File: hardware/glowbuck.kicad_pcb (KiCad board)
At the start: 4 copper layers, 80 x 50 mm, 126 parts, among them J1 Conn_01x04_Socket, J105 Conn_01x01_Pin, J106 Conn_01x01_Pin, J107 Conn_01x01_Pin, J201 USB_C_Receptacle_USB2.0_16P, J202 USB_C_Receptacle_USB2.0_16P, J3 Conn_02x08_Counter_Clockwise, Q401 2N7002NXAKR, SW101 SW_Push, SW102 SW_Push, U101 ESP32-S3-WROOM-1, U102 SN74LVC1T45DBV, U103 INA181A3, U201 TPS25730D, U202 TPD2E2U06DCK, U301 AP63203WU, U401 SIC437A

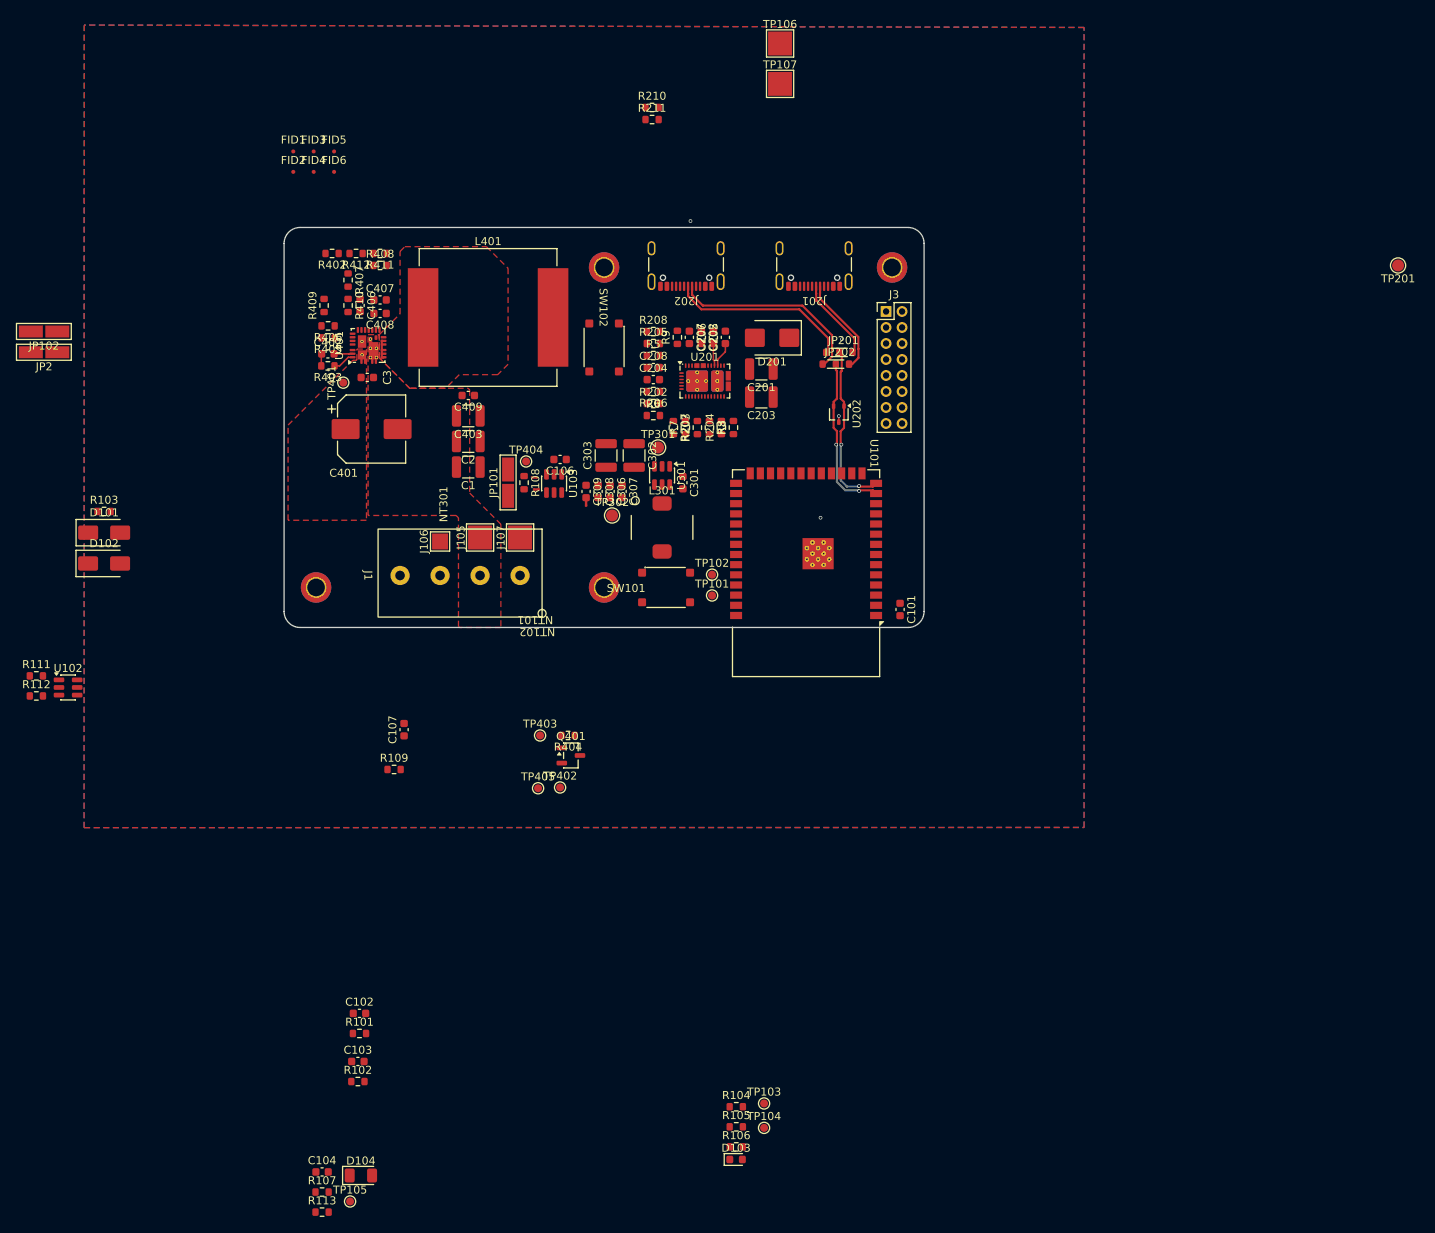
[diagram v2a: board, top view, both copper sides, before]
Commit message: Layout in progress. I2C done
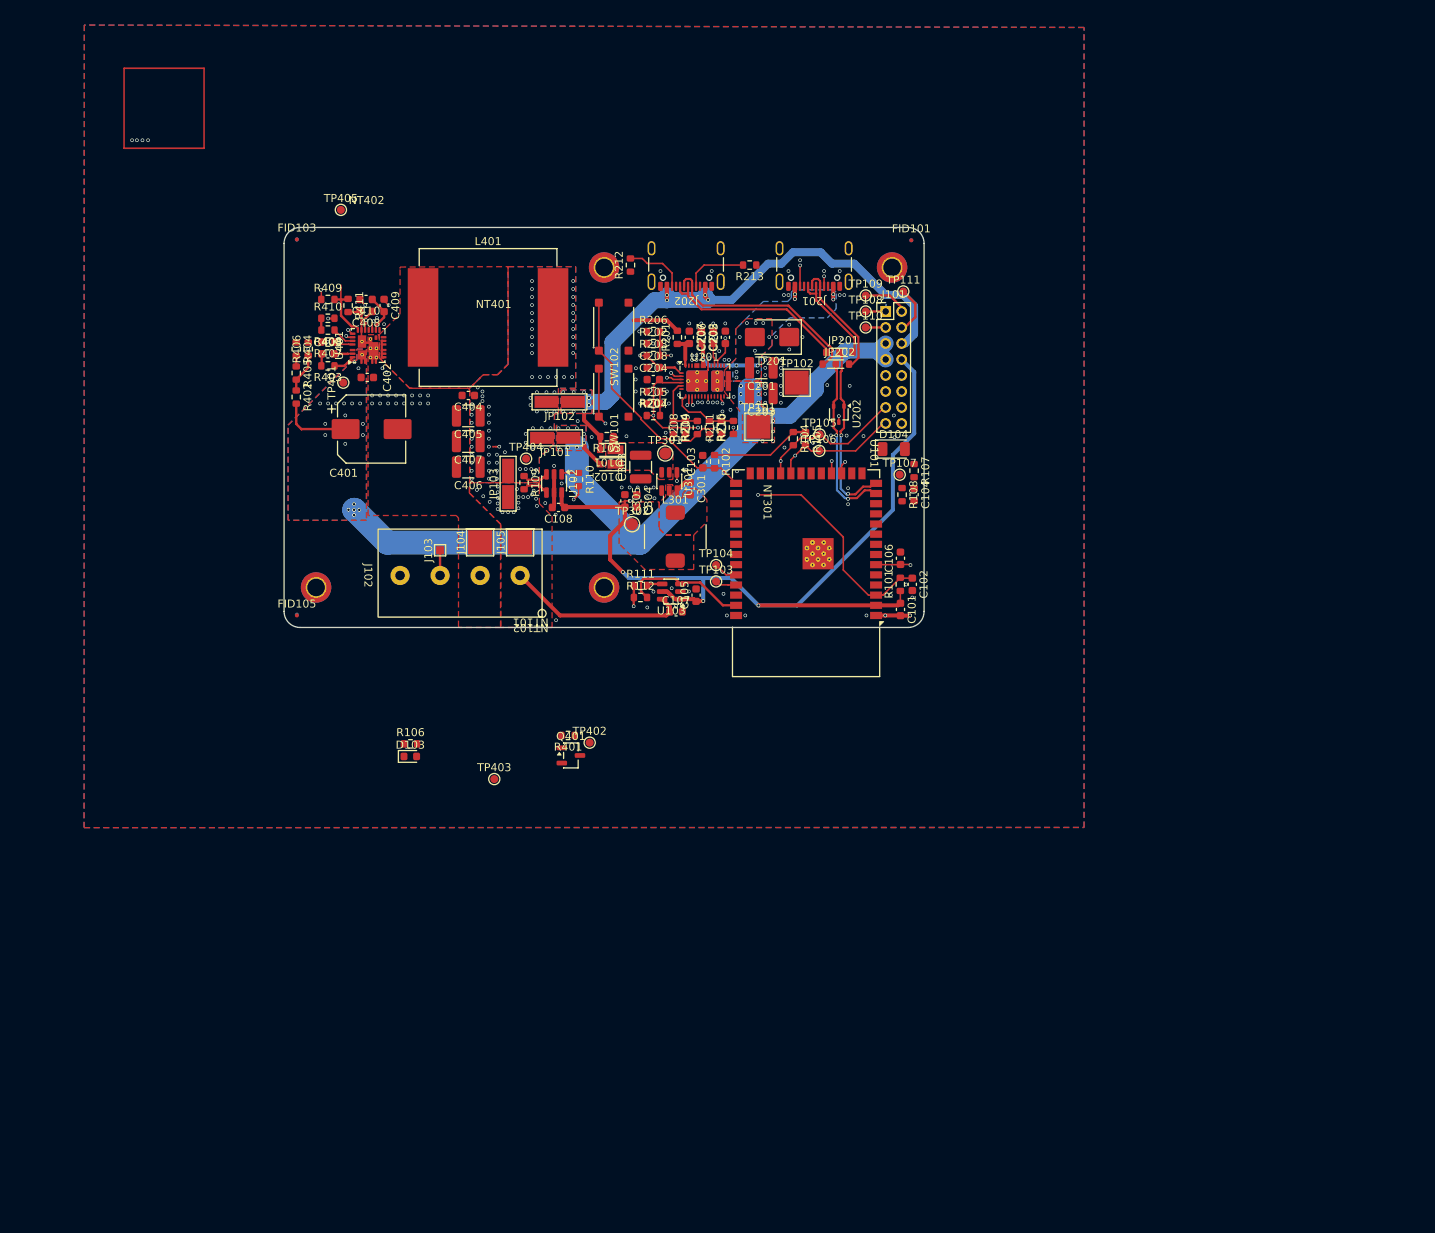
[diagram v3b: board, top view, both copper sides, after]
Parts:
- removed C302: 10u, Capacitor_SMD:C_1210_3225Metric
- removed C308, C309: 10u, Capacitor_SMD:C_0603_1608Metric
- removed J3: Conn_02x08_Counter_Clockwise, Connector_PinHeader_2.00mm:PinHeader_2x08_P2.00mm_Vertical
- removed TP201: TestPoint, TestPoint:TestPoint_Pad_D1.5mm
- added C105: 100n, Capacitor_SMD:C_0603_1608Metric, F.Cu at (105.5, 96.0)
- added C107: 100n, Capacitor_SMD:C_0603_1608Metric, F.Cu at (103.0, 98.0)
- added J101: Conn_02x08_Odd_Even, Connector_PinHeader_2.00mm:PinHeader_2x08_P2.00mm_Vertical, F.Cu at (129.2, 60.5)
- added NT401: NetTie_2, glowbuck:NETTIE_0.2mm, F.Cu at (80.3, 77.4)
- added NT402: NetTie_2, glowbuck:NETTIE_0.3mm, F.Cu at (64.4, 64.4)
- added TP108: TestPoint, TestPoint:TestPoint_Pad_D1.0mm, F.Cu at (126.7, 60.5)
- added TP109: TestPoint, TestPoint:TestPoint_Pad_D1.0mm, F.Cu at (126.7, 58.5)
- added TP110: TestPoint, TestPoint:TestPoint_Pad_D1.0mm, F.Cu at (126.7, 62.5)
- added TP111: TestPoint, TestPoint:TestPoint_Pad_D1.0mm, F.Cu at (131.4, 58.0)
- D101, D102: value SS34 -> MSS1P4-M3/89A; footprint Diode_SMD:D_SMA -> Diode_SMD:D_MicroSMP_AK
- FID102: renamed from FID4; moved to B.Cu
- FID104: renamed from FID5; moved to B.Cu
- FID106: renamed from FID6; moved to B.Cu
- J103: renamed from J106; footprint TestPoint:TestPoint_Pad_2.0x2.0mm -> TestPoint:TestPoint_Pad_1.0x1.0mm
- moved R107 118.6 mm to (132.8, 80.4), turned to -90 degrees
- moved TP107 113.9 mm to (130.9, 80.9)
- moved R108 113.4 mm to (131.2, 83.4), turned to -90 degrees
- moved D104 112.6 mm to (130.2, 77.7)
- moved C104 112.4 mm to (132.8, 83.4), turned to -90 degrees
- moved R102 89.4 mm to (107.8, 79.3), turned to -90 degrees
- moved R101 87.9 mm to (131.0, 94.6), turned to 90 degrees
- moved C102 87.5 mm to (132.5, 94.6), turned to -90 degrees
- moved C103 86.5 mm to (106.3, 79.3), turned to 90 degrees
- moved R105 86.5 mm to (119.2, 76.4), turned to -90 degrees
- moved TP106 84.9 mm to (120.9, 77.9)
- moved TP105 83.9 mm to (121.0, 75.9)
- moved R104 83.8 mm to (117.7, 76.4), turned to -90 degrees
- moved FID101 78.0 mm to (132.4, 51.6)
- moved R112 76.5 mm to (98.5, 96.2)
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- renumbered C107 to C106, C106 to C108, C307 to C304, C306 to C305, C3 to C402, C402 to C403, C409 to C404, C403 to C405, C1 to C406, C2 to C407, C406 to C408, C407 to C409, C408 to C410, FID1 to FID101, FID2 to FID103, FID3 to FID105, H1 to H101, H2 to H102, H3 to H103, H4 to H104, J1 to J102, J105 to J104, J107 to J105, JP2 to JP101, JP101 to JP103, R113 to R107, R107 to R108, R108 to R109, R109 to R110, R9 to R201, R205 to R202, R5 to R203, R6 to R204, R202 to R205, R208 to R206, R206 to R207, R7 to R208, R203 to R209, R8 to R210, R204 to R211, R210 to R212, R211 to R213, R207 to R214, R3 to R215, R404 to R401, R411 to R404, R412 to R405, R408 to R406, R405 to R407, R406 to R408, R407 to R409, R409 to R410, R410 to R411, TP106 to TP101, TP107 to TP102, TP101 to TP103, TP102 to TP104, TP103 to TP105, TP104 to TP106, TP105 to TP107, U103 to U102, U102 to U103
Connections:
- R409 pad 1: VOUT -> Net-(U401-V_{OUT})
- U101 pad 17: unconnected-(U101-IO9-Pad17) -> GPIO9
- U101 pad 18: unconnected-(U101-IO10-Pad18) -> GPIO10
- U101 pad 19: unconnected-(U101-IO11-Pad19) -> LIGHT_SENSE
- U101 pad 22: unconnected-(U101-IO14-Pad22) -> SCK
- U101 pad 23: unconnected-(U101-IO21-Pad23) -> SDA
- U101 pad 34: SDA -> unconnected-(U101-IO41-Pad34)
- U101 pad 35: SCK -> unconnected-(U101-IO42-Pad35)
- U101 pad 38: LIGHT_SENSE -> unconnected-(U101-IO2-Pad38)
- U101 pad 4: GPIO4 -> unconnected-(U101-IO4-Pad4)
- U101 pad 5: GPIO5 -> unconnected-(U101-IO5-Pad5)
- U103 pad 6: VOUT -> /LED_POW
- U401 pad 18: VOUT -> Net-(U401-V_{OUT})
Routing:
- net +3V3: track 0.00 -> 126.6 mm, vias 0 -> 3
- net VBUS: track 0.00 -> 112.9 mm, vias 0 -> 40
- net Net-(U401-V_{OUT}): track 0.00 -> 75.6 mm, vias 0 -> 3
- net +5V: track 0.00 -> 71.2 mm, vias 0 -> 12
- net /MC_EN: track 0.00 -> 59.3 mm, vias 0 -> 2
- net CURSENSE_V: track 0.00 -> 53.1 mm, vias 0 -> 2
- net SDA: track 0.00 -> 37.9 mm, vias 0 -> 2
- net SCK: track 0.00 -> 35.8 mm, vias 0 -> 2
- net /LED_D0: track 0.00 -> 32.1 mm, vias 0 -> 1
- net /MC_BOOT0: track 0.00 -> 32.0 mm
- net /USB-C and PD/PD_LDO1V5: track 0.00 -> 31.4 mm, vias 0 -> 4
- net /USB-C and PD/PD_LDO_3V3: track 0.00 -> 31.2 mm, vias 0 -> 6
- net /LED_POW: track 0.00 -> 23.0 mm, vias 0 -> 21
- net /USB-C and PD/USB_CC2: track 2.82 -> 21.4 mm, vias 0 -> 2
- net /USB-C and PD/USB_CC1: track 3.16 -> 20.9 mm, vias 0 -> 2
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- added copper zone on F.Cu, net +3V3
- added copper zone on B.Cu, net +5V
- added copper zone on F.Cu, net +5V
- added copper zone on F.Cu, net /Buck 3V3/SW
- added copper zone on F.Cu, net /Buck 3V3/VIN
- added copper zone on F.Cu, net /LED_POW
- added copper zone on B.Cu, net /USB-C and PD/VBUS_IN
- added copper zone on F.Cu, net /USB-C and PD/VBUS_IN
- added copper zone on B.Cu, net VBUS
- added copper zone on In2.Cu, net VBUS
- added copper zone on B.Cu, net VOUT
- added copper zone on F.Cu, net VOUT
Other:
- board text added: "glowbuck"
- board text added: "v1|Designed by Diamantenmine Manual & project files: github.com/Diamantenmine/glowbuck"

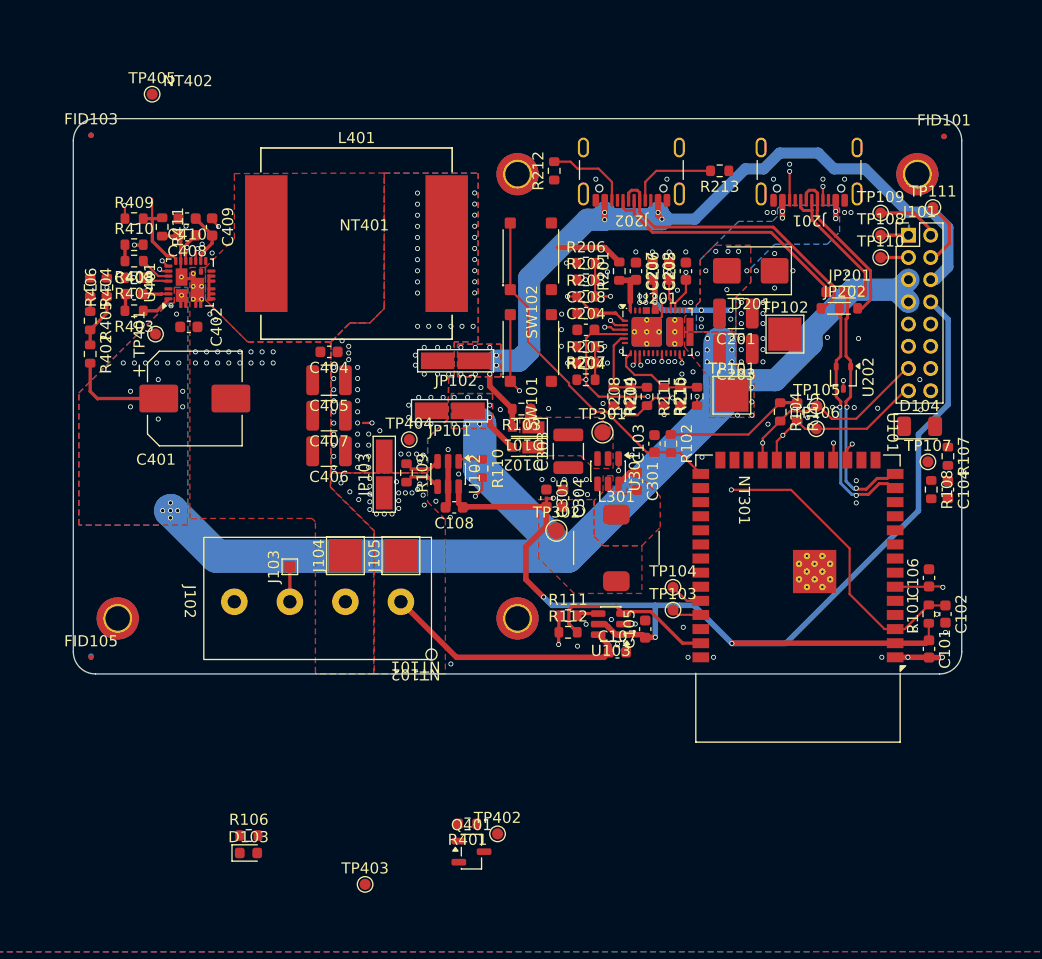
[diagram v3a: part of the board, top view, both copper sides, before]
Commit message: Fixed drc errors
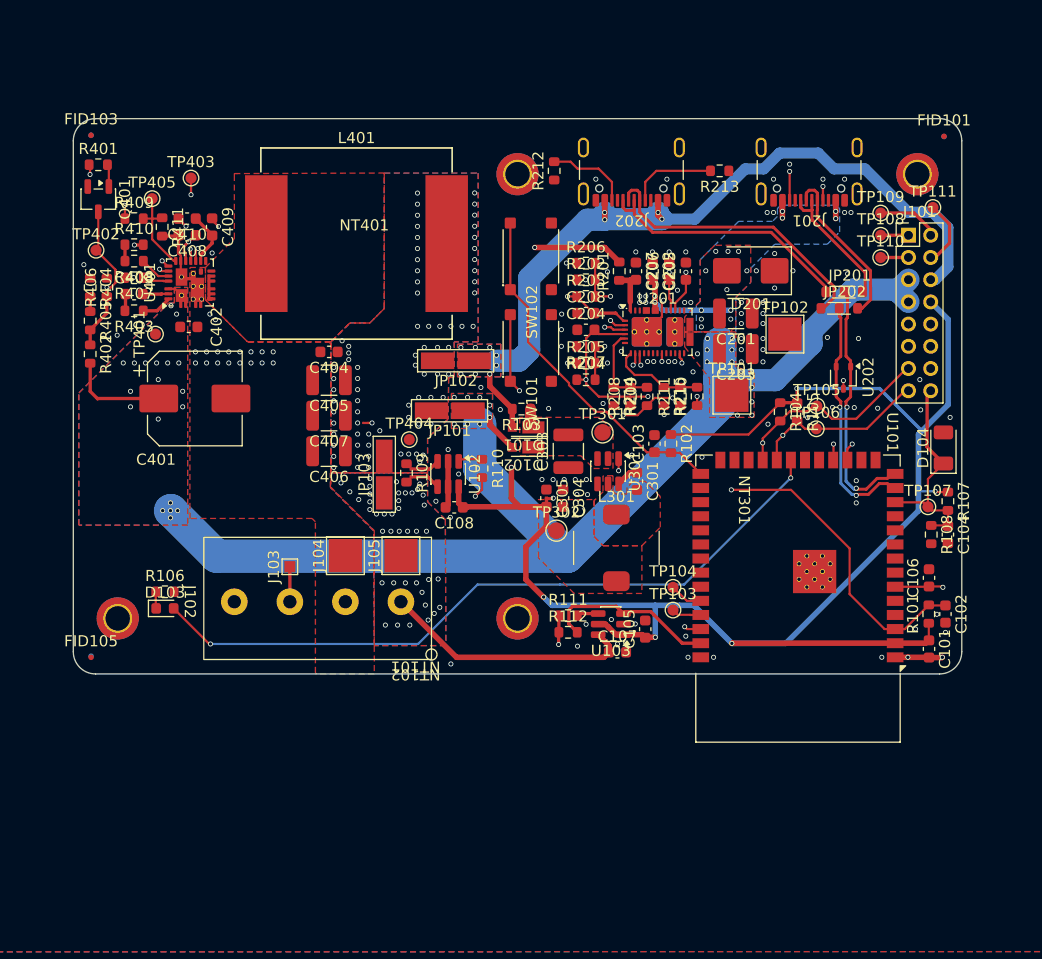
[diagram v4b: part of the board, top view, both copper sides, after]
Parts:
- moved R401 68.0 mm to (56.2, 54.1), turned to 0 degrees
- moved Q401 67.7 mm to (56.2, 57.2), turned to -90 degrees
- moved TP403 65.5 mm to (64.6, 55.4)
- moved TP402 63.8 mm to (56.0, 61.9)
- moved D103 23.3 mm to (62.2, 94.1)
- moved R106 23.2 mm to (62.2, 92.6)
- moved TP405 9.40 mm to (61.1, 57.2)
- moved C104 4.05 mm to (132.8, 87.5)
- moved R107 4.05 mm to (132.8, 84.5)
- moved R108 4.05 mm to (131.2, 87.5)
- moved TP107 4.05 mm to (130.9, 85.0)
- moved D104 2.90 mm to (132.3, 79.7), turned to 90 degrees
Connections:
- J101 pad 12: GND -> GPIO9
- J101 pad 14: GPIO9 -> GPIO10
- J101 pad 16: GPIO10 -> LIGHT_SENSE
- U101 pad 12: unconnected-(U101-IO8-Pad12) -> LIGHT_SENSE
- U101 pad 15: BUCK_DISABLE -> unconnected-(U101-IO3-Pad15)
- U101 pad 19: LIGHT_SENSE -> unconnected-(U101-IO11-Pad19)
- U101 pad 38: unconnected-(U101-IO2-Pad38) -> BUCK_DISABLE
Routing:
- net BUCK_DISABLE: track 0.00 -> 91.8 mm, vias 0 -> 2
- net /AUX_LED_GREEN: track 0.00 -> 64.7 mm, vias 0 -> 2
- net +3V3: track 126.6 -> 172.0 mm, vias 3 -> 7
- net LIGHT_SENSE: track 0.00 -> 19.8 mm
- net /Buck Power/PGOOD: track 0.00 -> 9.68 mm, vias 0 -> 2
- net /Buck Power/EN: track 12.1 -> 20.2 mm
- net GPIO10: track 12.2 -> 16.5 mm
- net GPIO9: track 14.9 -> 18.0 mm
- net Net-(Q401-G): track 0.00 -> 2.01 mm
- net Net-(D103-K): track 0.00 -> 1.52 mm
- net VBUS: track 112.9 -> 114.3 mm
- net Net-(J101-Pin_1): track 3.37 -> 2.50 mm
- net GND: vias 121 -> 123
- net /USB-C and PD/PD_LDO_3V3: vias 6 -> 5
- net /LED_POW: vias 21 -> 41
- added copper zone on B.Cu, net /LED_POW
- added copper zone on In2.Cu, net /LED_POW
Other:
- rule pad_to_mask_clearance: 0.1 -> 0
- board text added: "v1|Designed by Diamantenmine Manual & project files: github.com /Diamantenmine/glowbuck"
- board text removed: "v1|Designed by Diamantenmine Manual & project files: github.com/Diamantenmine/glowbuck"

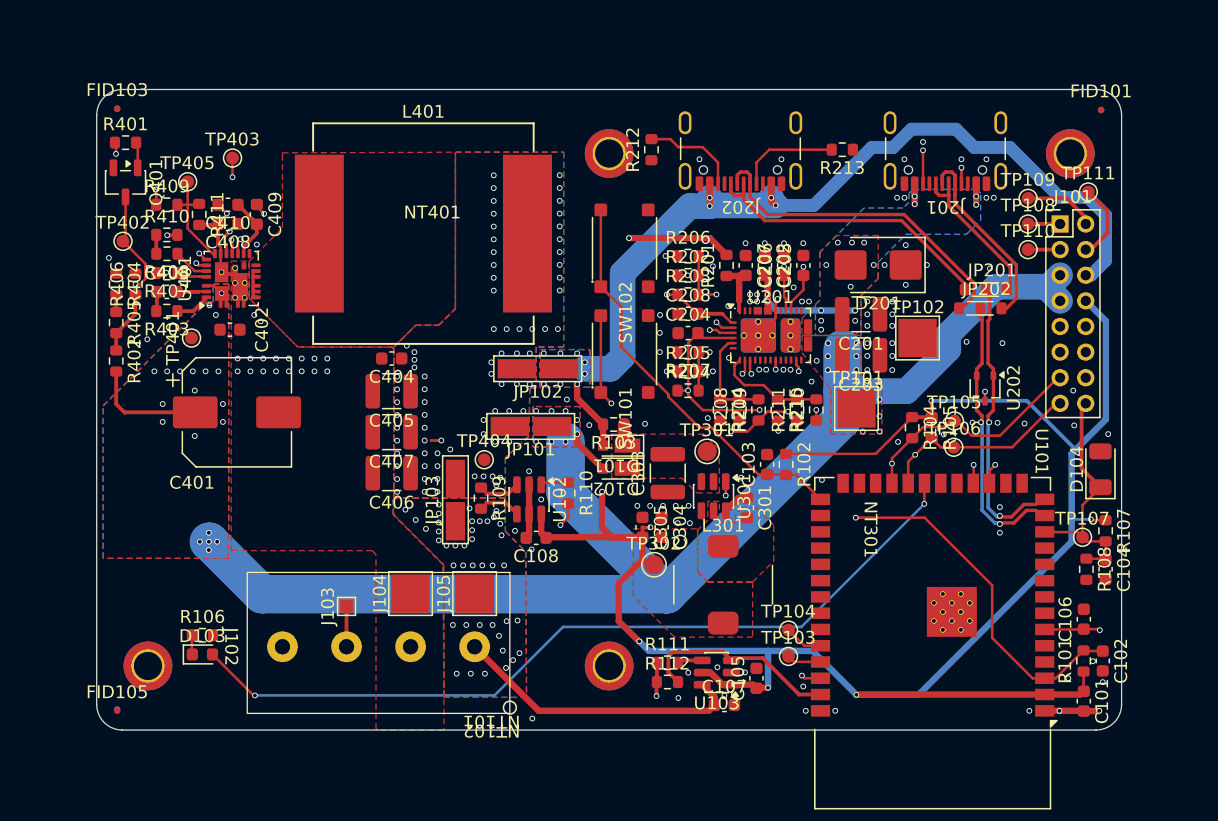
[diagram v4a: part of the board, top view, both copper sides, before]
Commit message: Fixed drc problems
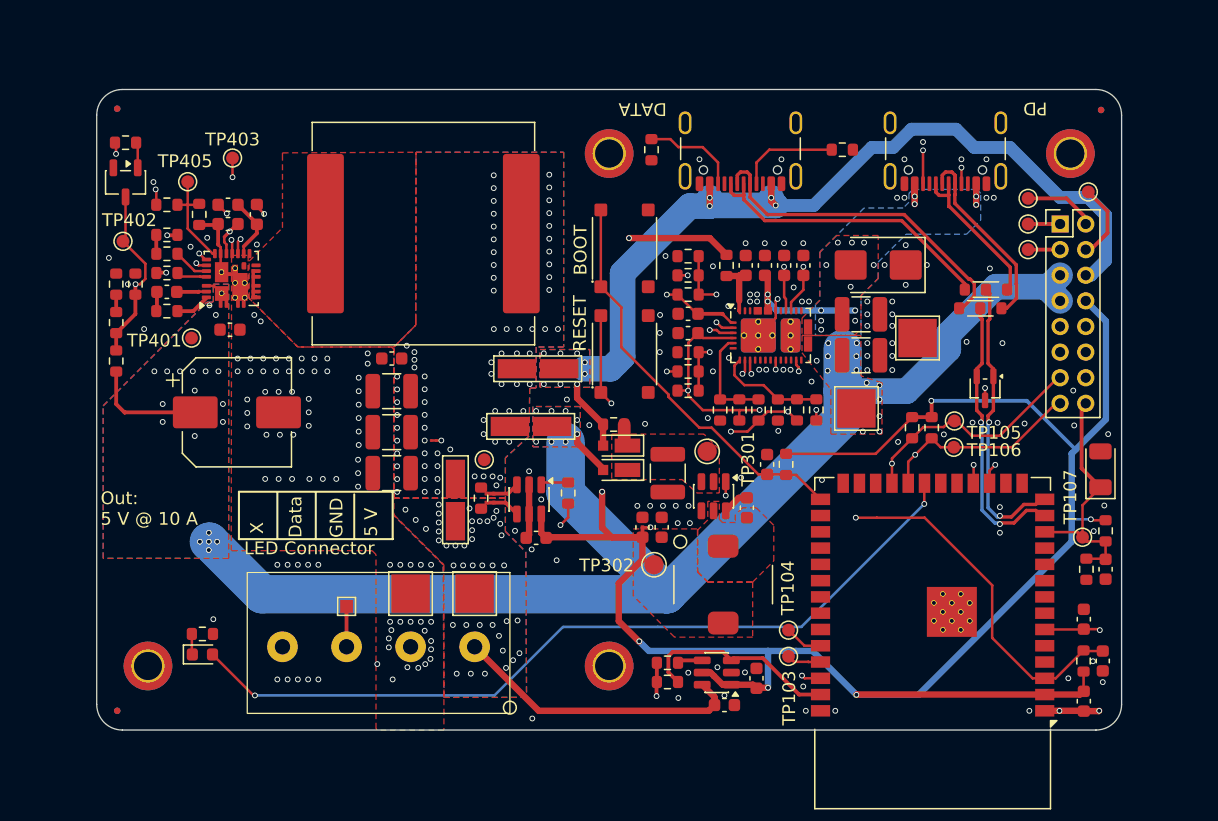
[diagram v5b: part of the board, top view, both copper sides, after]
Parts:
- moved D102 0.10 mm to (94.5, 79.7)
- moved FID106 0.10 mm to (55.6, 98.5)
- moved R106 0.10 mm to (62.2, 92.5)
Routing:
- net GND: track 16.6 -> 16.9 mm, vias 123 -> 192
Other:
- board text added: "5 V"
- board text added: "BOOT"
- board text added: "DATA"
- board text added: "Data"
- board text added: "GND"
- board text added: "LED Connector"
- board text added: "Out: 5 V @ 10 A"
- board text added: "PD"
- board text added: "RESET"
- board text added: "X"
